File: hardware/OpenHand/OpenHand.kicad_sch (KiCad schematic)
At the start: 80 parts, among them J1 CONN_MOTOR_1, J10 CONN_JTAG, J11 CONN_FDBK_2, J12 CONN_EMG_2, J13 CONN_POS_3, J2 CONN_MOTOR_2, J3 CONN_BATT, J4 CONN_POS_1, J5 USB_C_CONN, J6 CONN_MOTOR_3, J7 CONN_FDBK_1, J8 CONN_EMG_1, J9 CONN_POS_2, SW1 BTN_RST, SW2 BTN_BOOT, SW3 SW_Push, U1 STM32F103RETx

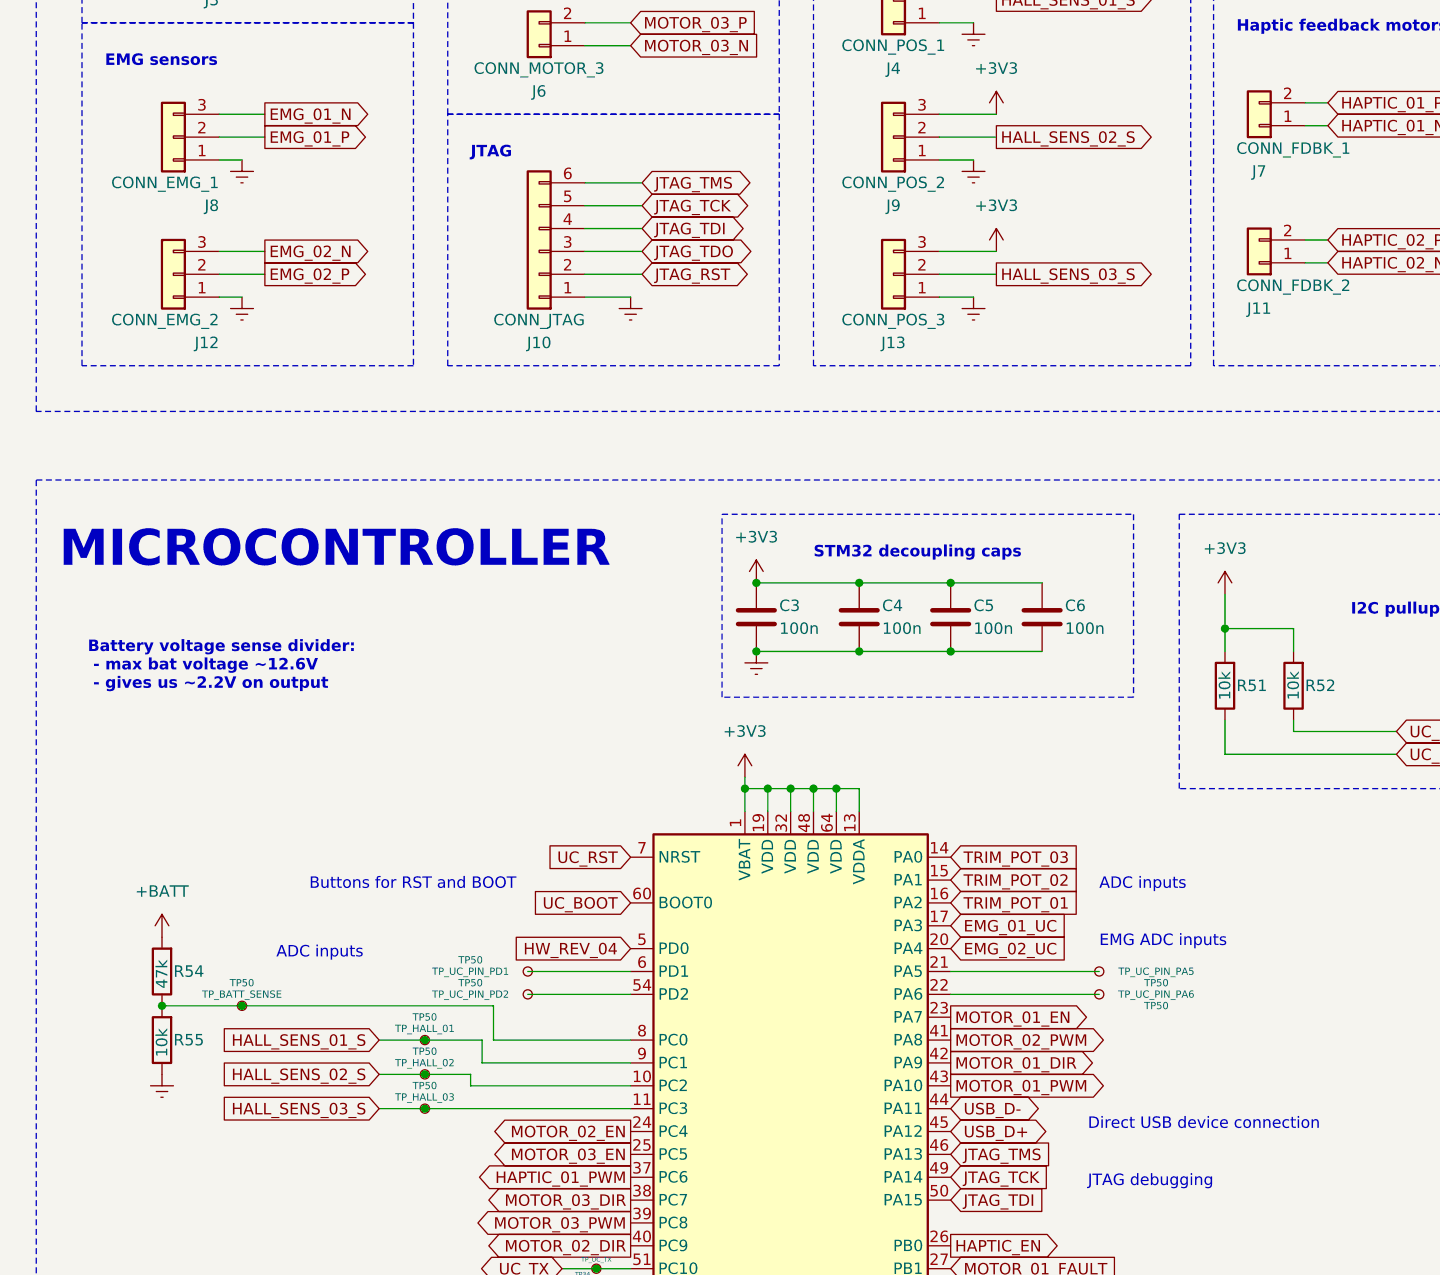
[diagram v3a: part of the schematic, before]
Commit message: Update PCB, add STLs from hand model
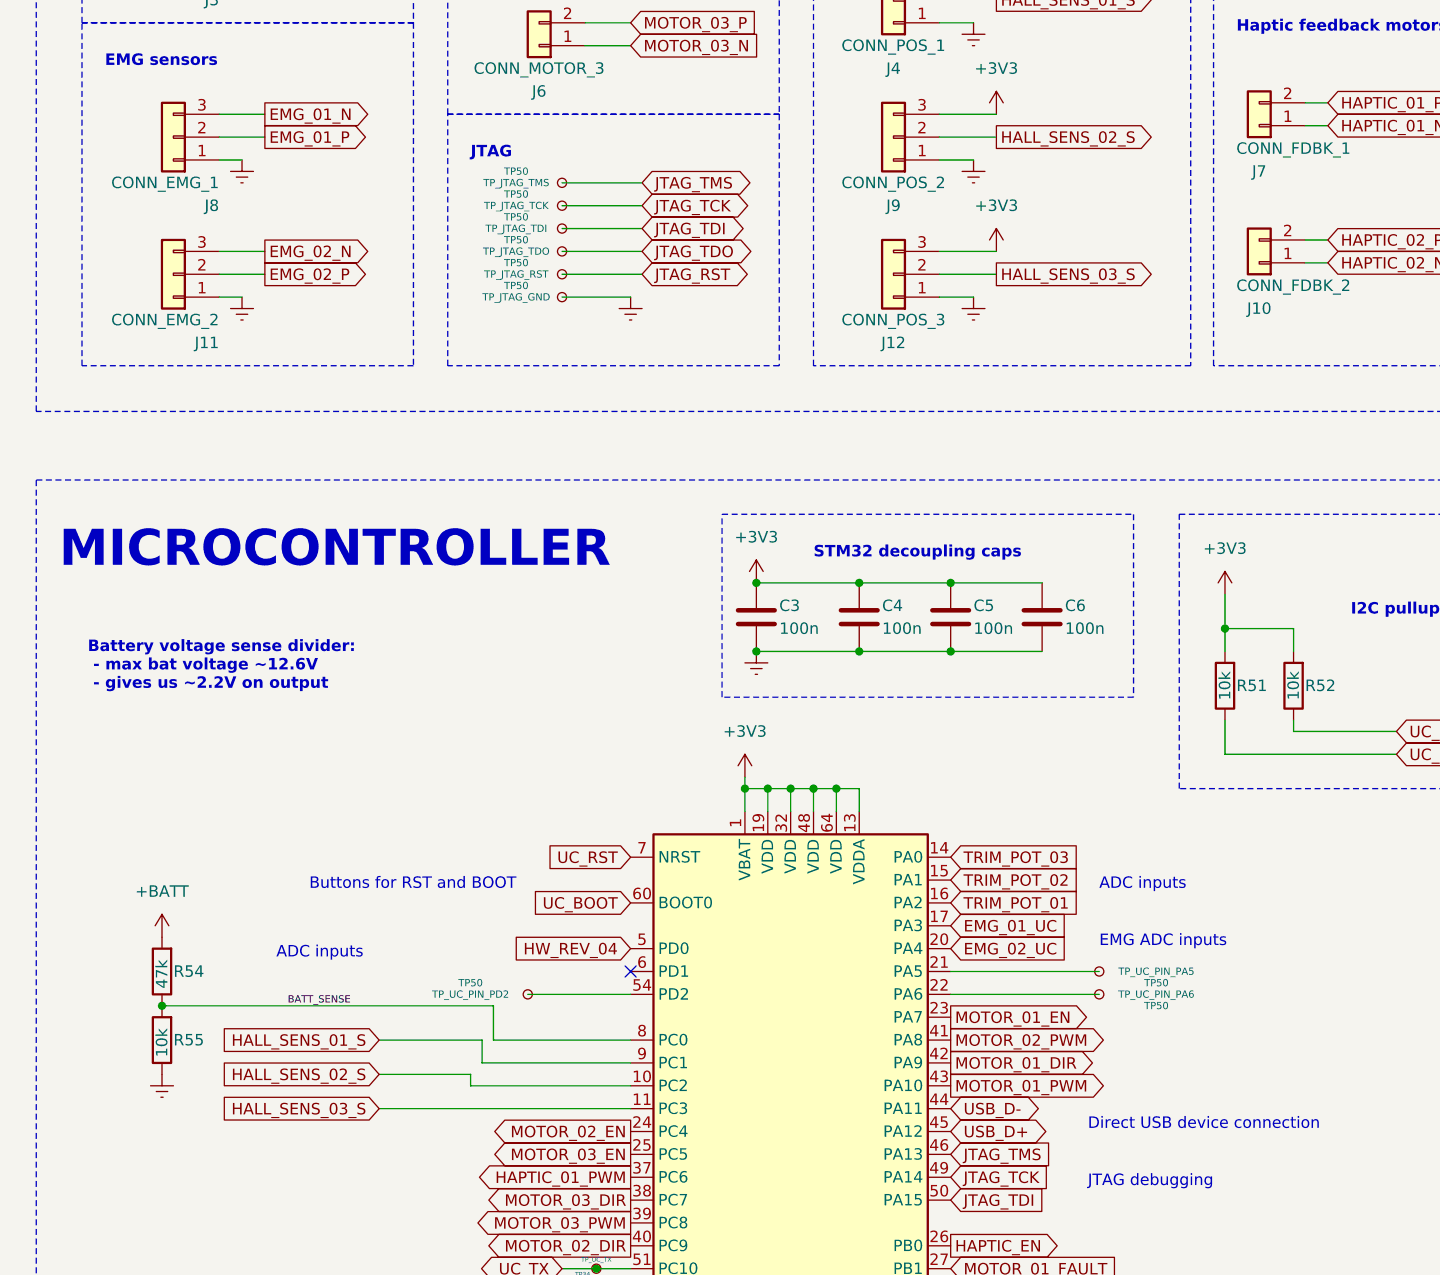
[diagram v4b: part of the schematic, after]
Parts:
- removed J10: CONN_JTAG, Connector_PinHeader_2.54mm:PinHeader_1x06_P2.54mm_Vertical, symbol Connector_Generic:Conn_01x06
- removed TP50: TP_BATT_SENSE, TestPoint:TestPoint_Pad_D1.0mm, symbol Connector:TestPoint_Small
- removed TP50: TP_HALL_03, TestPoint:TestPoint_Pad_D1.0mm, symbol Connector:TestPoint_Small
- removed TP50: TP_HALL_01, TestPoint:TestPoint_Pad_D1.0mm, symbol Connector:TestPoint_Small
- removed TP50: TP_UC_PIN_PD1, TestPoint:TestPoint_Pad_D1.0mm, symbol Connector:TestPoint_Small
- removed TP50: TP_HALL_02, TestPoint:TestPoint_Pad_D1.0mm, symbol Connector:TestPoint_Small
- added TP50: TP_JTAG_RST, TestPoint:TestPoint_Pad_D1.0mm, symbol Connector:TestPoint_Small
- added TP50: TP_JTAG_TDO, TestPoint:TestPoint_Pad_D1.0mm, symbol Connector:TestPoint_Small
- added TP50: TP_JTAG_TDI, TestPoint:TestPoint_Pad_D1.0mm, symbol Connector:TestPoint_Small
- added TP50: TP_JTAG_TCK, TestPoint:TestPoint_Pad_D1.0mm, symbol Connector:TestPoint_Small
- added TP50: TP_JTAG_TMS, TestPoint:TestPoint_Pad_D1.0mm, symbol Connector:TestPoint_Small
- added TP50: TP_JTAG_GND, TestPoint:TestPoint_Pad_D1.0mm, symbol Connector:TestPoint_Small
- renumbered J11 to J10, J12 to J11, J13 to J12
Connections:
- net Earth: now also TP50.1
- net JTAG_RST: now also TP50.1
- net JTAG_TCK: now also TP50.1
- net JTAG_TDI: now also TP50.1
- net JTAG_TDO: now also TP50.1
- net JTAG_TMS: now also TP50.1
- net BATT_SENSE: now reaches R54.1, R55.2, U1.8 (PC0)
- no-connect marks 3 -> 4

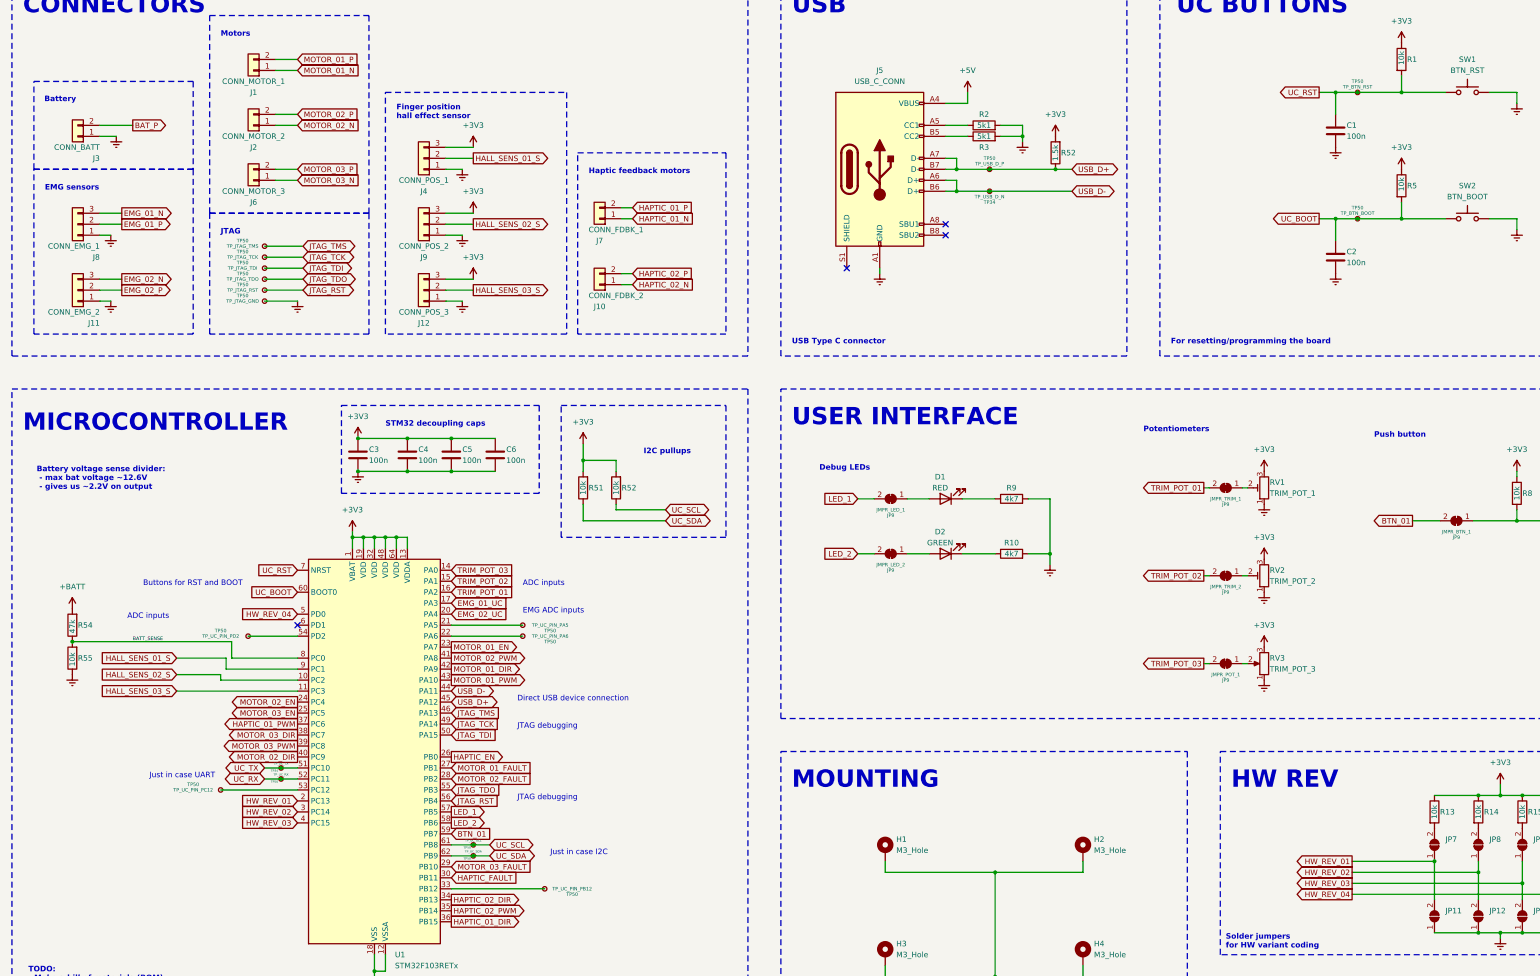
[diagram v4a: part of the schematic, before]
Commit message: Update to KiCAD 8 and order components from LCSC
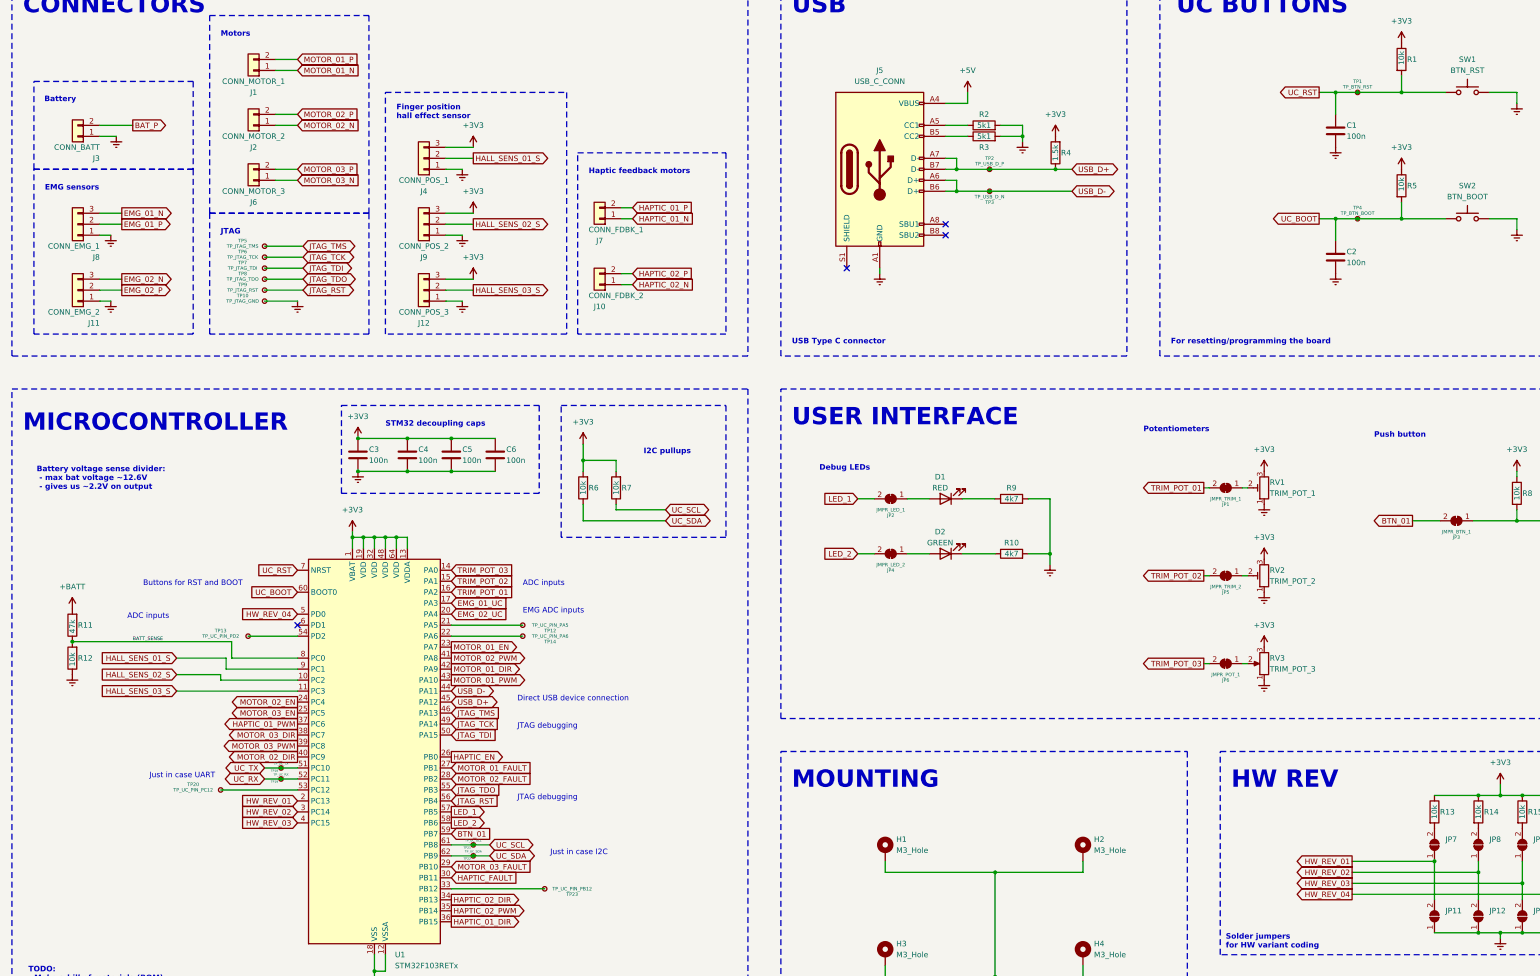
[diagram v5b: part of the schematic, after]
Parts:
- renumbered JP9 to JP1, JP9 to JP2, JP9 to JP3, JP9 to JP4, JP9 to JP5, JP9 to JP6, R54 to R11, R55 to R12, R52 to R4, R51 to R6, R52 to R7, TP50 to TP1, TP50 to TP10, TP50 to TP12, TP50 to TP13, TP50 to TP14, TP34 to TP18, TP50 to TP19, TP50 to TP2, TP50 to TP20, TP50 to TP21, TP50 to TP22, TP50 to TP23, TP34 to TP3, TP50 to TP4, TP50 to TP5, TP50 to TP6, TP50 to TP7, TP50 to TP8, TP50 to TP9
